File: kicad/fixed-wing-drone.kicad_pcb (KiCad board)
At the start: 2 copper layers, 95 x 60 mm, 28 parts, among them J1 1, J10 AUX POWER, J11 RC_POWER, J12 I2C, J13 EXTRA STEMMA QT, J14 I2C, J15 I2C, J16 AUX, J17 FC UBEC Input, J18 ESC UBEC Input, J19 Secondary ESC Input, J2 2, J3 3, J4 4, J5 5, J6 6, J7 RC_SIGNAL_IN, J8 LIDAR, J9 GPS, Q1 FC REV POLARITY PROT, Q2 ESC REV POLARITY PROT, U1 ESP32-S3-DevKitC

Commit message: updated gitignore and tried out some changes to pcb layout
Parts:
- added J20: LIDAR BKUP, Connector_PinHeader_2.54mm:PinHeader_1x04_P2.54mm_Vertical, F.Cu at (183.8, 119.8)
- J1, J17, J2, J3, J4, J5, J6: footprint Connector_PinHeader_2.54mm:PinHeader_1x03_P2.54mm_Vertical -> Connector_PinHeader_2.54mm:PinHeader_1x03_P2.54mm_Vertical_SMD_Pin1Left
- J10: value AUX POWER -> ACC POWER
- J11: value RC_POWER -> RC POWER OUT; footprint Connector_PinHeader_2.54mm:PinHeader_1x02_P2.54mm_Vertical -> Connector_PinHeader_2.54mm:PinHeader_1x02_P2.54mm_Vertical_SMD_Pin1Left
- J16: value AUX -> ACC IO
- J18: value ESC UBEC Input -> ESC UBEC; footprint Connector_PinHeader_2.54mm:PinHeader_1x03_P2.54mm_Vertical -> Connector_PinHeader_2.54mm:PinHeader_1x03_P2.54mm_Vertical_SMD_Pin1Left
- J19: value Secondary ESC Input -> Secondary ESC; footprint Connector_PinHeader_2.54mm:PinHeader_1x03_P2.54mm_Vertical -> Connector_PinHeader_2.54mm:PinHeader_1x03_P2.54mm_Vertical_SMD_Pin1Left
- J7: value RC_SIGNAL_IN -> RC SIGNAL IN; footprint Connector_PinHeader_2.54mm:PinHeader_1x06_P2.54mm_Vertical -> Connector_PinHeader_2.54mm:PinHeader_1x06_P2.54mm_Vertical_SMD_Pin1Left
- J8: footprint Connector_PinHeader_2.54mm:PinHeader_1x04_P2.54mm_Vertical -> Connector_Molex:Molex_PicoBlade_53398-0471_1x04-1MP_P1.25mm_Vertical
- J9: footprint Connector_PinHeader_2.54mm:PinHeader_1x04_P2.54mm_Vertical -> Connector_PinHeader_2.54mm:PinHeader_1x04_P2.54mm_Vertical_SMD_Pin1Left
- moved J17 6.45 mm to (139.0, 69.6), turned to -90 degrees
- moved J7 6.17 mm to (187.5, 93.9)
- moved J8 4.35 mm to (162.8, 120.0), turned to 180 degrees
- moved J4 4.25 mm to (139.2, 115.5)
- moved J6 4.21 mm to (124.7, 115.5)
- moved J1 3.65 mm to (166.0, 71.0)
- moved J5 3.58 mm to (131.9, 115.5)
- moved J9 3.04 mm to (162.7, 112.3)
- moved J15 3.04 mm to (174.0, 70.9)
- moved J18 2.61 mm to (183.2, 106.8)
- moved J16 2.25 mm to (102.8, 106.7)
- moved J19 2.24 mm to (182.8, 80.7)
- moved J12 2.18 mm to (150.2, 114.8)
- moved J3 1.80 mm to (152.0, 71.0)
- moved Q2 1.56 mm to (176.9, 113.0)
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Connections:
- J17 pad 2: GND -> Net-(J17-Pin_2)
- J17 pad 3: Net-(J17-Pin_3) -> GND
- J18 pad 2: GND -> Net-(J18-Pin_2)
- J18 pad 3: Net-(J18-Pin_3) -> GND
- J19 pad 2: GND -> unconnected-(J19-Pin_2-Pad2)
- J19 pad 3: unconnected-(J19-Pin_3-Pad3) -> GND
- J8 pad 1: GND -> /FC_5v
- J8 pad 2: +3V3 -> /LIDAR_TX
- J8 pad 3: /LIDAR_TX -> /LIDAR_RX
- J8 pad 4: /LIDAR_RX -> GND
- J9 pad 1: GND -> +3V3
- J9 pad 2: +3V3 -> GND
- Q1 pad 2: Net-(J17-Pin_3) -> Net-(J17-Pin_2)
- Q2 pad 2: Net-(J18-Pin_3) -> Net-(J18-Pin_2)
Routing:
- net /FC_5v: track 114.5 -> 189.1 mm
- net GND: track 248.7 -> 316.6 mm, vias 2 -> 4
- net /LIDAR_TX: track 17.4 -> 41.1 mm, vias 0 -> 2
- net /LIDAR_RX: track 18.3 -> 36.3 mm, vias 0 -> 2
- net Net-(J18-Pin_3): track 12.7 -> 0.00 mm
- net Net-(J18-Pin_2): track 0.00 -> 12.7 mm
- net /SDA: track 92.2 -> 98.7 mm
- net /SCL: track 91.9 -> 98.4 mm
- net Net-(J17-Pin_3): track 6.44 -> 0.00 mm
- net Net-(J17-Pin_2): track 0.00 -> 4.89 mm
- net /SERVO_OUT_6: track 9.43 -> 13.8 mm
- net /RECIEVER_4: track 58.9 -> 62.9 mm, vias 1 -> 2
- net /RECIEVER_6: track 41.6 -> 45.5 mm, vias 1 -> 2
- net /RECIEVER_2: track 45.8 -> 49.4 mm, vias 1 -> 2
- net /SERVO_5v: track 102.7 -> 99.6 mm
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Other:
- board size 95 x 60 mm -> 95 x 61.2 mm
- board text added: "August 2026"
- board text added: "Autonomous Fixed Wing Flight Controller v2.0"
- board text added: "GPS"
- board text added: "LIDAR"
- board text removed: "Autonomous Fixed Wing Flight Controller v1.0"
- board text removed: "June 2026"

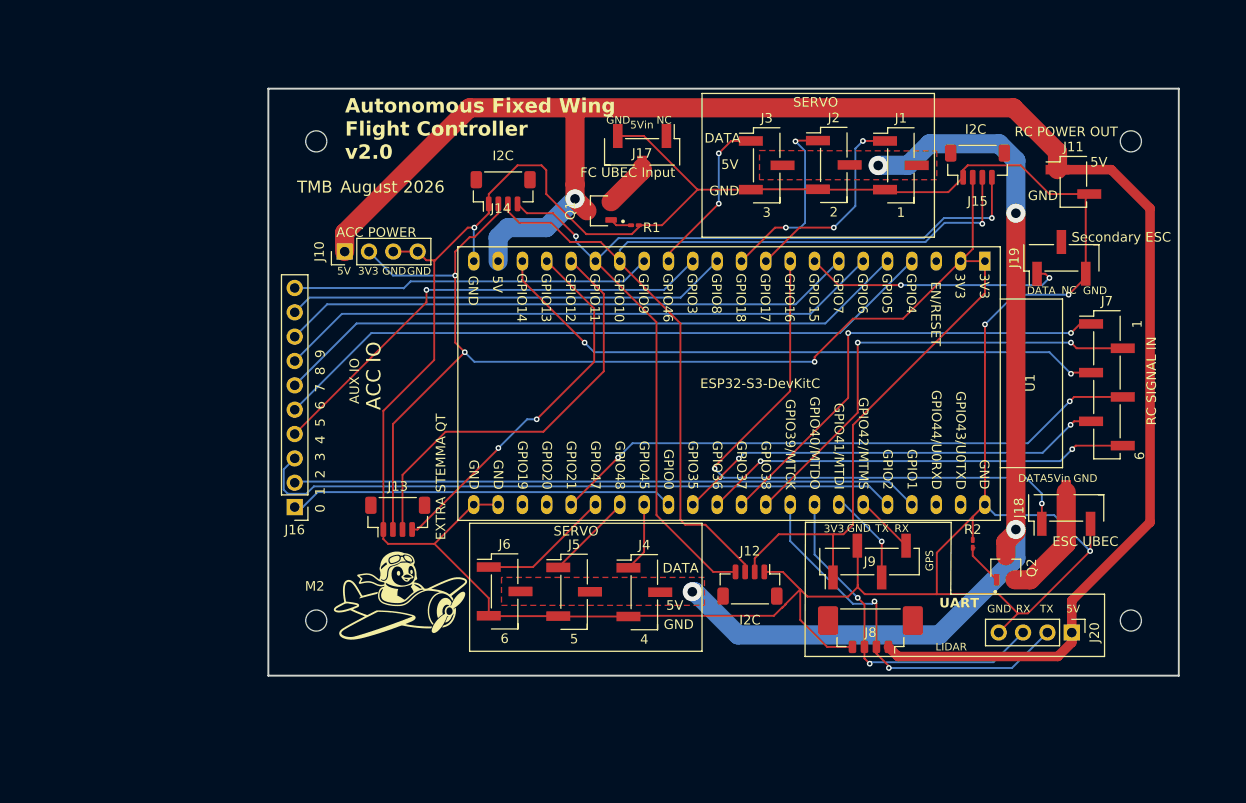
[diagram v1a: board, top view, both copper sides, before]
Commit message: V2 PCB; Fixed pin ordering, changed to mostly smd connectors, added 5v jst gh for lidar & airspeed; and fixed misprints on silkscreen
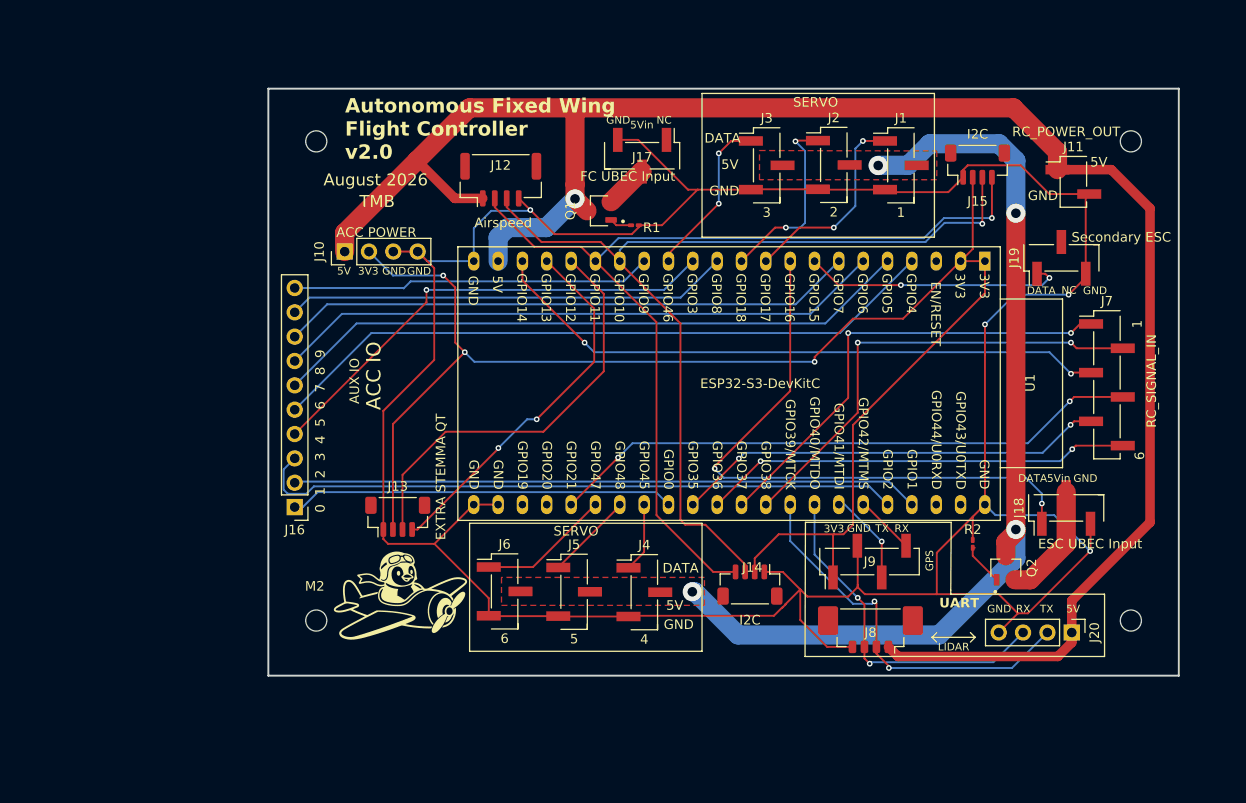
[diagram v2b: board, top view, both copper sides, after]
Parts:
- J11: value RC POWER OUT -> RC_POWER_OUT
- J12: value I2C -> Airspeed; footprint Connector_JST:JST_SH_BM04B-SRSS-TB_1x04-1MP_P1.00mm_Vertical -> Connector_JST:JST_GH_BM04B-GHS-TBT_1x04-1MP_P1.25mm_Vertical
- J18: value ESC UBEC -> ESC UBEC Input
- J7: value RC SIGNAL IN -> RC_SIGNAL_IN
- moved J12 49.6 mm to (124.2, 72.5), turned to 0 degrees
- moved J14 48.5 mm to (150.2, 114.8), turned to 180 degrees
- moved J17 0.41 mm to (139.0, 70.0)
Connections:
- J12 pad 1: GND -> /FC_5v
- J12 pad 2: +3V3 -> /SCL
- J12 pad 4: /SCL -> GND
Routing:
- net +3V3: track 169.6 -> 159.2 mm
- net /FC_5v: track 189.1 -> 197.6 mm
- net GND: track 316.6 -> 311.9 mm
- net /SCL: track 98.4 -> 101.2 mm, vias 2 -> 1

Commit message: Reverted to through hole but added new connectors for airspeed and added 5v for powering it. Did other minor revisions like removing some of the extra AUX IO
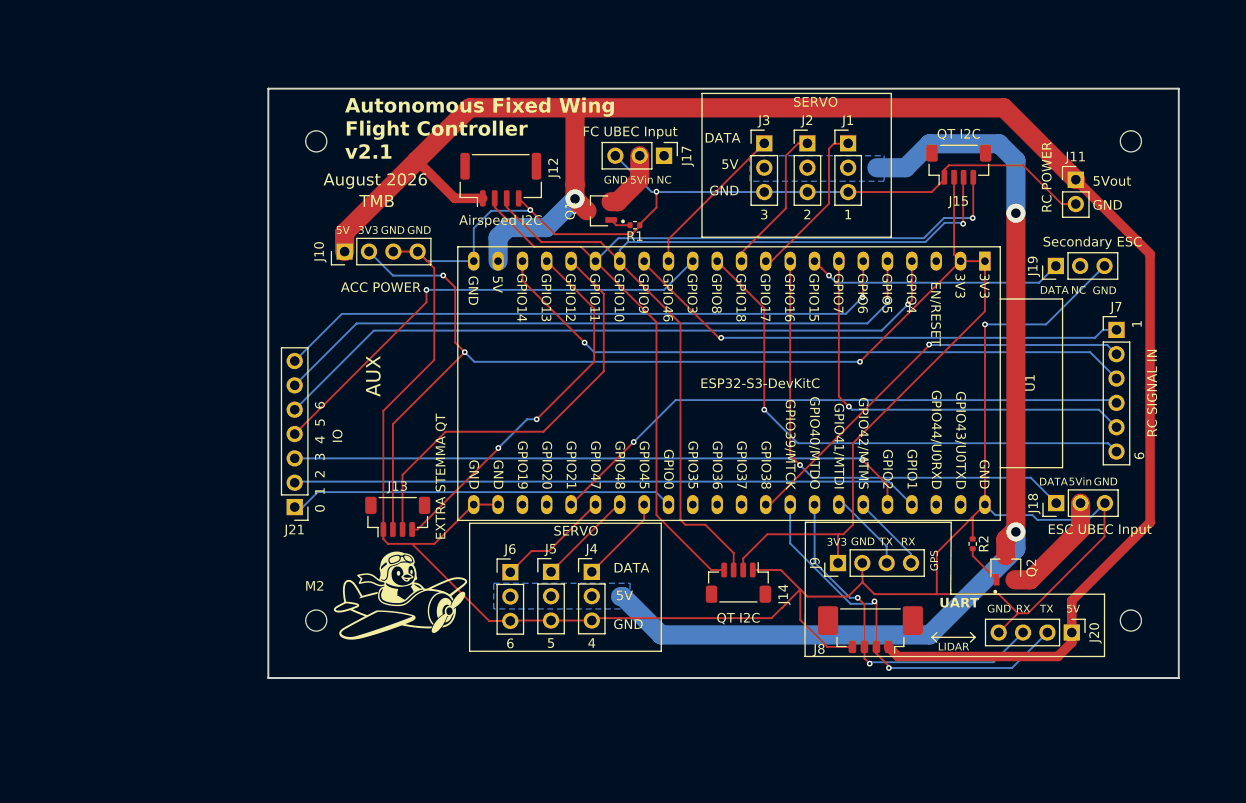
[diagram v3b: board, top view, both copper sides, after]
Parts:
- removed J16: ACC IO, Connector_PinHeader_2.54mm:PinHeader_1x10_P2.54mm_Vertical
- added J21: AUX, Connector_PinHeader_2.54mm:PinHeader_1x07_P2.54mm_Vertical, F.Cu at (102.8, 106.7)
- J1, J17, J18, J19, J2, J3, J4, J5, J6: footprint Connector_PinHeader_2.54mm:PinHeader_1x03_P2.54mm_Vertical_SMD_Pin1Left -> Connector_PinHeader_2.54mm:PinHeader_1x03_P2.54mm_Vertical
- J11: value RC_POWER_OUT -> RC POWER; footprint Connector_PinHeader_2.54mm:PinHeader_1x02_P2.54mm_Vertical_SMD_Pin1Left -> Connector_PinHeader_2.54mm:PinHeader_1x02_P2.54mm_Vertical
- J12: value Airspeed -> Airspeed I2C
- J14, J15: value I2C -> QT I2C
- J7: value RC_SIGNAL_IN -> RC SIGNAL IN; footprint Connector_PinHeader_2.54mm:PinHeader_1x06_P2.54mm_Vertical_SMD_Pin1Left -> Connector_PinHeader_2.54mm:PinHeader_1x06_P2.54mm_Vertical
- J9: footprint Connector_PinHeader_2.54mm:PinHeader_1x04_P2.54mm_Vertical_SMD_Pin1Left -> Connector_PinHeader_2.54mm:PinHeader_1x04_P2.54mm_Vertical
- R1, R2: footprint Resistor_SMD:R_0201_0603Metric_Pad0.64x0.40mm_HandSolder -> Resistor_SMD:R_0402_1005Metric
- moved J1 5.96 mm to (160.5, 68.7)
- moved J4 5.88 mm to (133.8, 113.4)
- moved J7 5.82 mm to (188.5, 88.2)
- moved J2 3.55 mm to (156.2, 68.7)
- moved J9 3.29 mm to (159.4, 112.5)
- moved J5 3.18 mm to (129.5, 113.4)
- moved J3 2.30 mm to (151.8, 68.7)
- moved J17 2.29 mm to (141.3, 70.0)
- moved J6 2.09 mm to (125.2, 113.5)
- moved J15 1.95 mm to (172.1, 70.9)
- moved J14 1.22 mm to (149.1, 114.5)
- moved J18 1.15 mm to (182.2, 106.2)
- moved J19 1.02 mm to (182.2, 81.5)
- moved J11 0.34 mm to (184.2, 72.5)
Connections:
- U1 pad 12: /ACC_8 -> /RECIEVER_6
- U1 pad 15: /ACC_9 -> /RECIEVER_1
- U1 pad 32: /RECIEVER_5 -> unconnected-(U1-GPIO35-Pad32)
- U1 pad 33: /RECIEVER_6 -> unconnected-(U1-GPIO36-Pad33)
- U1 pad 34: /RECIEVER_1 -> unconnected-(U1-GPIO37-Pad34)
- U1 pad 7: /ACC_7 -> /RECIEVER_5
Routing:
- net /ACC_7: track 60.0 -> 0.00 mm
- net /ACC_8: track 46.3 -> 0.00 mm
- net /ACC_9: track 37.7 -> 0.00 mm
- net /PRIMARY_ESC_SIGNAL: track 63.3 -> 50.1 mm, vias 2 -> 1
- net /RECIEVER_6: track 45.5 -> 56.1 mm, vias 2 -> 1
- net /SERVO_5v: track 99.6 -> 106.5 mm, vias 4 -> 2
- net GND: track 311.9 -> 305.8 mm, vias 4 -> 3
- net /RECIEVER_2: track 49.4 -> 44.0 mm, vias 2 -> 1
- net /RECIEVER_1: track 48.8 -> 53.1 mm, vias 2 -> 1
- net /SERVO_OUT_1: track 21.1 -> 17.0 mm, vias 2 -> 0
- net /SERVO_OUT_2: track 19.9 -> 16.0 mm, vias 2 -> 0
- net /FC_5v: track 197.6 -> 193.7 mm
- net /SDA: track 99.2 -> 95.9 mm
- net /SCL: track 101.2 -> 98.0 mm
- net /ACC_2: track 68.0 -> 65.1 mm, vias 0 -> 1
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- added copper zone on B.Cu, net /SERVO_5v
- removed copper zone on F.Cu, net /SERVO_5v
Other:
- board size 95 x 61.2 mm -> 95 x 61.5 mm
- board text added: "0 1 2 3 4 5 6"
- board text added: "5Vout"
- board text added: "Autonomous Fixed Wing Flight Controller v2.1"
- board text added: "IO"
- board text removed: "0 1 2 3 4 5 6 7 8 9"
- board text removed: "AUX IO"
- board text removed: "Autonomous Fixed Wing Flight Controller v2.0"

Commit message: PCB v3.0
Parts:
- removed J12: Airspeed I2C, Connector_JST:JST_GH_BM04B-GHS-TBT_1x04-1MP_P1.25mm_Vertical
- removed J17: FC UBEC Input, Connector_PinHeader_2.54mm:PinHeader_1x03_P2.54mm_Vertical
- removed J18: ESC UBEC Input, Connector_PinHeader_2.54mm:PinHeader_1x03_P2.54mm_Vertical
- removed J21: AUX, Connector_PinHeader_2.54mm:PinHeader_1x07_P2.54mm_Vertical
- removed REF** (x4): MountingHole_2.2mm_M2, MountingHole:MountingHole_2.2mm_M2
- added C1: 100nF, Capacitor_SMD:C_0402_1005Metric, F.Cu at (130.5, 94.8)
- added C10: 22uF, Capacitor_SMD:C_0805_2012Metric, F.Cu at (113.2, 65.0)
- added C11: 100nF, Capacitor_SMD:C_0402_1005Metric, F.Cu at (115.2, 65.0)
- added C12: 1uF, Capacitor_SMD:C_0402_1005Metric, F.Cu at (111.2, 109.8)
- added C13: 100nF, Capacitor_SMD:C_0402_1005Metric, F.Cu at (160.5, 68.0)
- added C14: 100nF, Capacitor_SMD:C_0402_1005Metric, F.Cu at (111.2, 108.8)
- added C15: 100nF, Capacitor_SMD:C_0402_1005Metric, F.Cu at (140.5, 91.5)
- added C16: 100nF, Capacitor_SMD:C_0402_1005Metric, F.Cu at (138.5, 93.2)
- added C2: 2.2 uF, Capacitor_SMD:C_0603_1608Metric, F.Cu at (131.8, 94.8)
- added C3: 10 nF, Capacitor_SMD:C_0402_1005Metric, F.Cu at (128.0, 95.8)
- added C4: 100nF, Capacitor_SMD:C_0402_1005Metric, F.Cu at (156.8, 92.5)
- added C5: 100nF, Capacitor_SMD:C_0402_1005Metric, F.Cu at (151.2, 93.0)
- added C6: 1uF, Capacitor_SMD:C_0402_1005Metric, F.Cu at (105.0, 65.2)
- added C7: 1uF, Capacitor_SMD:C_0402_1005Metric, F.Cu at (110.8, 65.2)
- added C8: 1uF, Capacitor_SMD:C_0402_1005Metric, F.Cu at (124.5, 102.2)
- added C9: 1uF, Capacitor_SMD:C_0402_1005Metric, F.Cu at (118.8, 101.2)
- added Card1: MicroSD, easyeda2kicad:TF-SMD_XKTF-001B, F.Cu at (152.5, 72.1)
- added D1: Status LED, LED_SMD:LED_0603_1608Metric, F.Cu at (119.3, 87.7)
- added D2: Power LED, LED_SMD:LED_0603_1608Metric, F.Cu at (111.0, 71.8)
- added D3: B5819W, Diode_SMD:D_SOD-123, F.Cu at (105.2, 73.0)
- added D5: B5819W, Diode_SMD:D_SOD-123, F.Cu at (111.0, 101.0)
- added J16: 8, Connector_Molex:Molex_KK-254_AE-6410-03A_1x03_P2.54mm_Vertical, F.Cu at (171.3, 108.2)
- added J22: ESC1, Connector_Molex:Molex_KK-254_AE-6410-03A_1x03_P2.54mm_Vertical, F.Cu at (179.0, 75.5)
- added L1: Ferrite Bead, easyeda2kicad:L0603, F.Cu at (138.1, 109.3)
- added L2: Ferrite Bead, easyeda2kicad:L0603, F.Cu at (148.0, 111.0)
- added L4: Ferrite Bead, easyeda2kicad:L0603, F.Cu at (141.0, 100.5)
- added M2: MountingHole_2.2mm_M2, MountingHole:MountingHole_2.2mm_M2, F.Cu at (114.5, 118.2)
- added M2: MountingHole_2.2mm_M2, MountingHole:MountingHole_2.2mm_M2, F.Cu at (173.0, 67.8)
- added M2: MountingHole_2.2mm_M2, MountingHole:MountingHole_2.2mm_M2, F.Cu at (173.0, 118.2)
- added R10: 100K, Resistor_SMD:R_0402_1005Metric, F.Cu at (183.8, 80.2)
- added R11: 10K, Resistor_SMD:R_0402_1005Metric, F.Cu at (156.8, 81.2)
- added R12: 330R, Resistor_SMD:R_0402_1005Metric, F.Cu at (138.0, 68.6)
- added R13: 330R, Resistor_SMD:R_0402_1005Metric, F.Cu at (138.0, 69.9)
- added R14: 330R, Resistor_SMD:R_0402_1005Metric, F.Cu at (138.0, 72.4)
- added R15: 330R, Resistor_SMD:R_0402_1005Metric, F.Cu at (138.0, 74.8)
- added R16: 330R, Resistor_SMD:R_0402_1005Metric, F.Cu at (137.2, 85.2)
- added R17: 330R, Resistor_SMD:R_0402_1005Metric, F.Cu at (138.0, 73.5)
- added R18: 330R, Resistor_SMD:R_0402_1005Metric, F.Cu at (138.0, 71.1)
- added R19: 330R, Resistor_SMD:R_0402_1005Metric, F.Cu at (137.2, 86.2)
- added R20: 6.8K, Resistor_SMD:R_0402_1005Metric, F.Cu at (127.8, 100.8)
- added R21: 6.8K, Resistor_SMD:R_0402_1005Metric, F.Cu at (129.0, 102.0)
- added R22: 330R, Resistor_SMD:R_0402_1005Metric, F.Cu at (138.0, 64.8)
- added R23: 330R, Resistor_SMD:R_0402_1005Metric, F.Cu at (138.0, 66.1)
- added R3: 5.1K, Resistor_SMD:R_0402_1005Metric, F.Cu at (108.8, 78.5)
- added R4: 5.1K, Resistor_SMD:R_0402_1005Metric, F.Cu at (108.8, 81.8)
- added R5: 220R, Resistor_SMD:R_0402_1005Metric, F.Cu at (119.2, 86.2)
- added R6: 220R, Resistor_SMD:R_0402_1005Metric, F.Cu at (111.0, 70.2)
- added R7: 10k, Resistor_SMD:R_0402_1005Metric, F.Cu at (116.0, 66.5)
- added R8: 100K, Resistor_SMD:R_0402_1005Metric, F.Cu at (105.0, 93.5)
- added R9: 100R, Resistor_SMD:R_0402_1005Metric, F.Cu at (111.0, 114.8)
- added SW1: TS-1088, Button_Switch_SMD:SW_SPST_TS-1088-xR020, F.Cu at (107.3, 109.0)
- added SW2: TS-1088, Button_Switch_SMD:SW_SPST_TS-1088-xR020, F.Cu at (107.2, 115.2)
- added U2: Primary IMU, easyeda2kicad:LGA-14_L3.0-W2.5-P0.50-TL, F.Cu at (128.3, 93.5)
- added U3: Backup IMU, easyeda2kicad:LGA-16_L4.5-W3.0-P0.50-BL, F.Cu at (154.4, 92.5)
- added U5: AP2112K-3.3, Package_TO_SOT_SMD:SOT-23-5, F.Cu at (108.0, 65.8)
- added U6: AP2112K-3.3, Package_TO_SOT_SMD:SOT-23-5, F.Cu at (121.6, 102.8)
- added U7: Barometer, easyeda2kicad:LGA-8_L2.5-W2.0-P0.65-TR_DPS368, F.Cu at (141.1, 93.5)
- J1, J2, J3, J4, J5, J6: footprint Connector_PinHeader_2.54mm:PinHeader_1x03_P2.54mm_Vertical -> Connector_Molex:Molex_KK-254_AE-6410-03A_1x03_P2.54mm_Vertical
- J10: value ACC POWER -> UWB SPI; footprint Connector_PinHeader_2.54mm:PinHeader_1x04_P2.54mm_Vertical -> Connector_JST:JST_GH_BM07B-GHS-TBT_1x07-1MP_P1.25mm_Vertical
- J11: value RC POWER -> Inter ESP UART; footprint Connector_PinHeader_2.54mm:PinHeader_1x02_P2.54mm_Vertical -> Connector_JST:JST_GH_BM03B-GHS-TBT_1x03-1MP_P1.25mm_Vertical
- J13: value EXTRA STEMMA QT -> USB-C; footprint Connector_JST:JST_SH_BM04B-SRSS-TB_1x04-1MP_P1.00mm_Vertical -> Connector_USB:USB_C_Receptacle_GCT_USB4105-xx-A_16P_TopMnt_Horizontal
- J14: value QT I2C -> GPS/Compass; footprint Connector_JST:JST_SH_BM04B-SRSS-TB_1x04-1MP_P1.00mm_Vertical -> Connector_JST:JST_GH_BM06B-GHS-TBT_1x06-1MP_P1.25mm_Vertical
- J15: value QT I2C -> Airspeed I2C; footprint Connector_JST:JST_SH_BM04B-SRSS-TB_1x04-1MP_P1.00mm_Vertical -> Connector_JST:JST_GH_BM04B-GHS-TBT_1x04-1MP_P1.25mm_Vertical
- J19: value Secondary ESC -> ESC2; footprint Connector_PinHeader_2.54mm:PinHeader_1x03_P2.54mm_Vertical -> Connector_Molex:Molex_KK-254_AE-6410-03A_1x03_P2.54mm_Vertical
- J20: value LIDAR BKUP -> FC UBEC Input; footprint Connector_PinHeader_2.54mm:PinHeader_1x04_P2.54mm_Vertical -> Connector_Molex:Molex_KK-254_AE-6410-03A_1x03_P2.54mm_Vertical
- J7: value RC SIGNAL IN -> RC Conn; footprint Connector_PinHeader_2.54mm:PinHeader_1x06_P2.54mm_Vertical -> Connector_Molex:Molex_KK-254_AE-6410-03A_1x03_P2.54mm_Vertical
- J8: value LIDAR -> LIDAR I2C
- J9: value GPS -> 7; footprint Connector_PinHeader_2.54mm:PinHeader_1x04_P2.54mm_Vertical -> Connector_Molex:Molex_KK-254_AE-6410-03A_1x03_P2.54mm_Vertical
- Q1: value FC REV POLARITY PROT -> reverse polarity protection; footprint AO3407A:SOT95P280X125-3N -> easyeda2kicad:SOT-23-3_L2.9-W1.6-P1.90-LS2.8-BR
- Q2: value ESC REV POLARITY PROT -> reverse polarity protection; footprint AO3407A:SOT95P280X125-3N -> easyeda2kicad:SOT-23-3_L2.9-W1.6-P1.90-LS2.8-BR
- R1, R2: value 100K -> 10K
- U1: value ESP32-S3-DevKitC -> ESP32-S3-WROOM-1; footprint PCM_Espressif:ESP32-S3-DevKitC-trav-snf2 -> easyeda2kicad:WIRELM-SMD_ESP32-S3-WROOM-1
- moved J20 82.2 mm to (103.8, 101.3), turned to 90 degrees
- moved J11 74.4 mm to (123.0, 114.7), turned to 180 degrees
- moved J5 50.9 mm to (180.3, 115.3)
- moved J10 50.6 mm to (152.5, 104.0), turned to 180 degrees
- moved J6 49.9 mm to (171.3, 94.2)
- moved U1 48.7 mm to (126.8, 72.4), turned to 0 degrees
- moved J15 48.5 mm to (136.8, 104.2), turned to 180 degrees
- moved J4 46.8 mm to (180.3, 108.3)
- moved R2 43.4 mm to (161.8, 68.8)
- moved J3 43.3 mm to (180.3, 101.3)
- moved J2 35.1 mm to (180.3, 94.3)
- moved Q1 32.2 mm to (109.5, 96.0)
- moved Q2 31.9 mm to (180.3, 81.2)
- moved J13 29.7 mm to (102.7, 80.0), turned to -90 degrees
- moved J1 27.1 mm to (180.3, 87.3)
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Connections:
- J1 pad 1: /SERVO_OUT_1 -> Net-(J1-Pin_1)
- J1 pad 2: /SERVO_5v -> /actuator_io/esc_io/SERVO_5V
- J10 pad 1: /FC_5v -> /SENSOR_3V3
- J10 pad 2: +3V3 -> /MOSI
- J10 pad 3: GND -> /MISO
- J10 pad 4: GND -> /SCK
- J11 pad 1: /FC_5v -> GND
- J11 pad 2: GND -> /INTER_ESP_TX
- J14 pad 1: GND -> /SDA
- J14 pad 2: +3V3 -> GND
- J14 pad 3: /SDA -> /GPS_RX
- J14 pad 4: /SCL -> /GPS_TX
- J15 pad 1: GND -> Net-(J15-Pin_1)
- J15 pad 2: +3V3 -> /SCL
- J15 pad 4: /SCL -> GND
- J19 pad 1: /SECONDARY_ESC_SIGNAL -> Net-(J19-Pin_1)
- J2 pad 1: /SERVO_OUT_2 -> Net-(J2-Pin_1)
- J2 pad 2: /SERVO_5v -> /actuator_io/esc_io/SERVO_5V
- J20 pad 1: /FC_5v -> unconnected-(J20-Pin_1-Pad1)
- J20 pad 2: /LIDAR_TX -> Net-(J20-Pin_2)
- J20 pad 3: /LIDAR_RX -> GND
- J3 pad 1: /SERVO_OUT_3 -> Net-(J3-Pin_1)
- J3 pad 2: /SERVO_5v -> /actuator_io/esc_io/SERVO_5V
- J4 pad 1: /SERVO_OUT_4 -> Net-(J4-Pin_1)
- J4 pad 2: /SERVO_5v -> /actuator_io/esc_io/SERVO_5V
- J5 pad 1: /SERVO_OUT_5 -> Net-(J5-Pin_1)
- J5 pad 2: /SERVO_5v -> /actuator_io/esc_io/SERVO_5V
- J6 pad 1: /SERVO_OUT_6 -> Net-(J6-Pin_1)
- J6 pad 2: /SERVO_5v -> /actuator_io/esc_io/SERVO_5V
- J7 pad 1: /RECIEVER_1 -> /RC_SBUS
- J7 pad 2: /RECIEVER_2 -> /actuator_io/esc_io/SERVO_5V
- J7 pad 3: /RECIEVER_3 -> GND
- J8 pad 1: /FC_5v -> Net-(J8-Pin_1)
- J8 pad 2: /LIDAR_TX -> /SCL
- J8 pad 3: /LIDAR_RX -> /SDA
- J9 pad 1: +3V3 -> Net-(J9-Pin_1)
- J9 pad 2: GND -> /actuator_io/esc_io/SERVO_5V
- J9 pad 3: /GPS_TX -> GND
- Q1 pad 1: Net-(Q1-Pad1) -> Net-(Q1-G)
- Q1 pad 2: Net-(J17-Pin_2) -> Net-(J20-Pin_2)
- Q1 pad 3: /FC_5v -> Net-(D5-A)
- Q2 pad 1: Net-(Q2-Pad1) -> Net-(Q2-G)
- Q2 pad 3: /SERVO_5v -> /actuator_io/esc_io/SERVO_5V
- R1 pad 1: GND -> /ESP_3V3
- R1 pad 2: Net-(Q1-Pad1) -> Net-(Card1-DAT2)
- R2 pad 1: GND -> /ESP_3V3
- R2 pad 2: Net-(Q2-Pad1) -> Net-(Card1-DAT1)
- U1 pad 1: +3V3 -> GND
- U1 pad 10: /SERVO_OUT_1 -> /BAROMETER_CS
- U1 pad 11: /SERVO_OUT_2 -> /IMU1_CS
- U1 pad 12: /RECIEVER_6 -> /SD_CS
- U1 pad 13: /ACC_3 -> /esp32s3/DATA-
- U1 pad 14: /SERVO_OUT_3 -> /esp32s3/DATA+
- U1 pad 15: /RECIEVER_1 -> /GPS_RX
- U1 pad 16: /SDA -> /STATUS_LED
- U1 pad 17: /SCL -> /GPS_TX
- U1 pad 18: /EXTRA_QT_YELLOW -> /SDA
- U1 pad 19: /EXTRA_QT_BLUE -> /SCL
- U1 pad 2: +3V3 -> /ESP_3V3
- U1 pad 20: /RECIEVER_3 -> /IMU1_INT
- U1 pad 21: /FC_5v -> /UWB_INT
- U1 pad 22: GND -> /SCK
- U1 pad 23: GND -> /MISO
- U1 pad 24: GND -> /MOSI
- U1 pad 25: unconnected-(U1-GPIO19/USB_D--Pad25) -> /SERVO_OUT5
- U1 pad 26: unconnected-(U1-GPIO20/USB_D+-Pad26) -> /SERVO_OUT8
- U1 pad 27: /RECIEVER_4 -> /esp32s3/BOOT
- U1 pad 28: /SERVO_OUT_6 -> unconnected-(U1-IO35-Pad28)
- U1 pad 29: /SERVO_OUT_5 -> unconnected-(U1-IO36-Pad29)
- U1 pad 3: unconnected-(U1-CHIP_PU-Pad3) -> /esp32s3/EN
- U1 pad 30: /SERVO_OUT_4 -> unconnected-(U1-IO37-Pad30)
- U1 pad 31: /ACC_0 -> /SERVO_OUT4
- U1 pad 32: unconnected-(U1-GPIO35-Pad32) -> /SERVO_OUT7
- U1 pad 33: unconnected-(U1-GPIO36-Pad33) -> /SERVO_OUT3
- U1 pad 34: unconnected-(U1-GPIO37-Pad34) -> /SERVO_OUT6
- U1 pad 35: /RECIEVER_2 -> /SERVO_OUT2
- U1 pad 36: /LIDAR_TX -> /SERVO_OUT1
- U1 pad 37: /LIDAR_RX -> /RC_SBUS
- U1 pad 38: /GPS_TX -> /ESC_OUT1
- U1 pad 39: /GPS_RX -> /ESC_OUT2
- U1 pad 4: /ACC_4 -> /SD_CARD_DETECT
- U1 pad 40: /ACC_2 -> GND
- U1 pad 41: /ACC_1 -> GND
- U1 pad 5: /ACC_5 -> /INTER_ESP_RX
- U1 pad 6: /ACC_6 -> /INTER_ESP_TX
- U1 pad 7: /RECIEVER_5 -> /IMU2_GYRO_CS
- U1 pad 8: /SECONDARY_ESC_SIGNAL -> /IMU2_ACCEL_CS
- U1 pad 9: /PRIMARY_ESC_SIGNAL -> /UWB_CS
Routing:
- net GND: track 305.8 -> 96.1 mm, vias 3 -> 93
- net /FC_5v: track 193.7 -> 0.00 mm, vias 1 -> 0
- net +3V3: track 158.5 -> 0.00 mm, vias 3 -> 0
- net /SERVO_5v: track 106.5 -> 0.00 mm, vias 2 -> 0
- net /MISO: track 0.00 -> 105.7 mm, vias 0 -> 9
- net /SENSOR_3V3: track 0.00 -> 88.4 mm, vias 0 -> 2
- net /MOSI: track 0.00 -> 86.0 mm, vias 0 -> 4
- net /ESP_3V3: track 0.00 -> 84.7 mm, vias 0 -> 3
- net /SCK: track 0.00 -> 76.7 mm, vias 0 -> 4
- net /ACC_4: track 73.2 -> 0.00 mm, vias 1 -> 0
- net /ACC_5: track 69.9 -> 0.00 mm, vias 1 -> 0
- net /RECIEVER_3: track 68.2 -> 0.00 mm, vias 1 -> 0
- net /ACC_6: track 65.8 -> 0.00 mm, vias 1 -> 0
- net /ACC_1: track 65.4 -> 0.00 mm
- net /ACC_2: track 65.1 -> 0.00 mm, vias 1 -> 0
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- added copper zone on B.Cu, net /FC_5V
- added copper zone on F.Cu, net /FC_5V
- added copper zone on In2.Cu, net /FC_5V
- added copper zone on F.Cu, net /SENSOR_3V3
- added copper zone on F.Cu, net /actuator_io/esc_io/SERVO_5V
- added copper zone on In2.Cu, net /actuator_io/esc_io/SERVO_5V
- added copper zone on B.Cu, net GND
- added copper zone on F.Cu, net GND
- added copper zone on In1.Cu, net GND
- removed copper zone on B.Cu, net /SERVO_5v
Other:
- board size 95 x 61.5 mm -> 91 x 61.5 mm
- copper layers 2 -> 4
- board text added: "1 3"
- board text added: "1 4"
- board text added: "1 6"
- board text added: "4 1"
- board text added: "61.5mm"
- board text added: "7 1"
- board text added: "91mm"
- board text added: "Autonomous Fixed Wing Flight Controller v3.0"
- board text added: "C9"
- board text added: "DAT"
- board text added: "Power Plane Split"
- board text added: "September 2026"
- board text removed: "0 1 2 3 4 5 6"
- board text removed: "1"
- board text removed: "3V3"
- board text removed: "5Vin"
- board text removed: "5Vout"
- board text removed: "6"
- board text removed: "August 2026"
- board text removed: "Autonomous Fixed Wing Flight Controller v2.1"
- board text removed: "GPS"
- board text removed: "IO"
- board text removed: "LIDAR"
- board text removed: "M2"
- board text removed: "NC"
- board text removed: "RX"
- board text removed: "SERVO"
- board text removed: "TX"
- board text removed: "UART"
